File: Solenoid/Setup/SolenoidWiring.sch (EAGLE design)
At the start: 11 parts

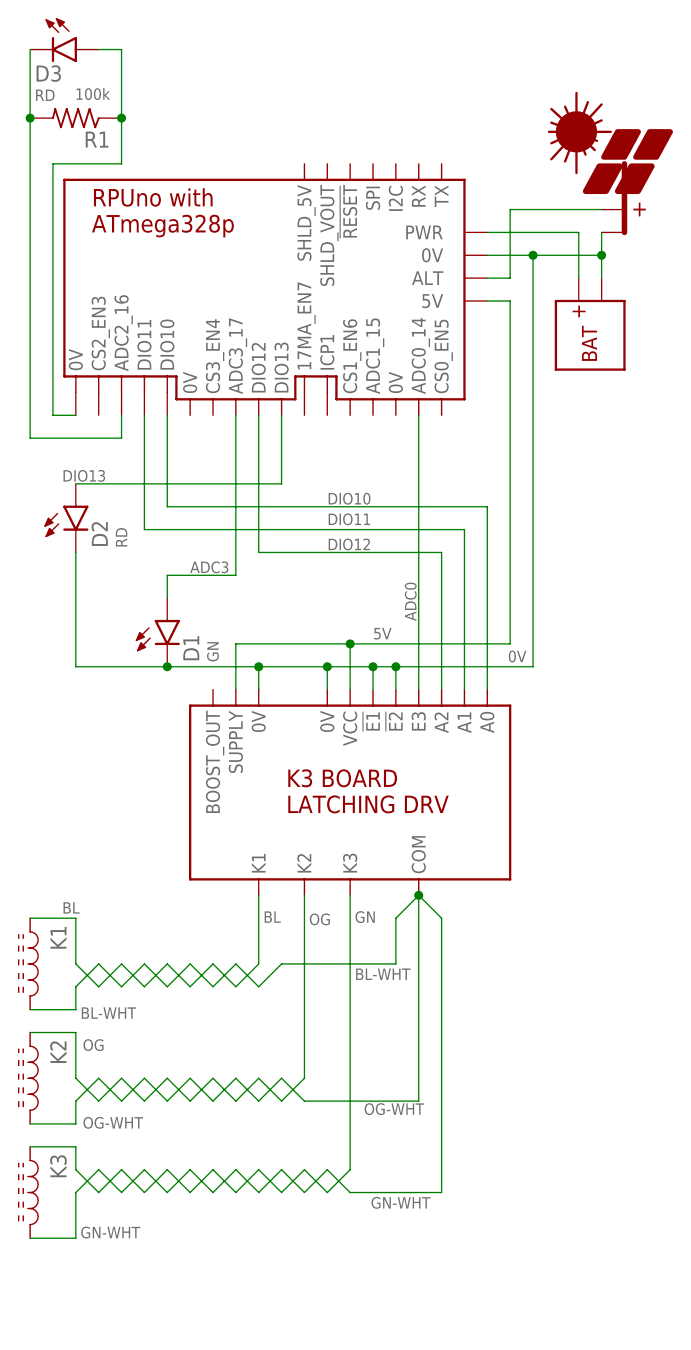
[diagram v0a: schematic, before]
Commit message: Solenoid: wiring show flow sensor
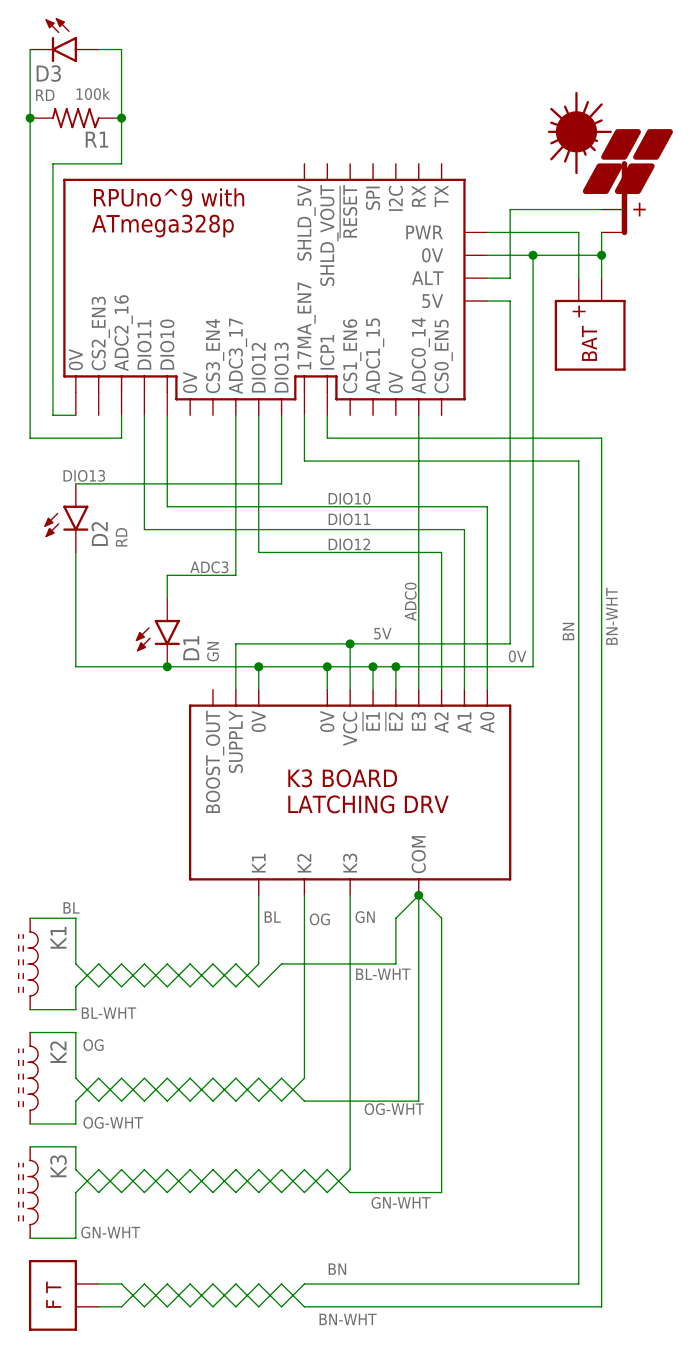
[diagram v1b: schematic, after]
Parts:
- added U$2: FT, Documentation:FT
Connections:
- new net BN: BM1.17MA_EN7, U$2.PWR
- new net BN-WHT: BM1.ICP1, U$2.PL
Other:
- note added: "FLOW SENSOR"
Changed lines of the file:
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@@
 <part name="D3" library="D-LED" deviceset="LED" device="5MM" value="RD"/>
 <part name="R1" library="R-C" deviceset="R" device="0805" value="100k"/>
+<part name="U$2" library="Documentation" deviceset="FT" device=""/>
 </parts>
 <sheets>
@@
 <text x="20.828" y="67.564" size="1.27" layer="98" rot="R90">DAY-NIGHT</text>
 <text x="8.89" y="116.84" size="1.27" layer="98" rot="R90">LIGHT SENSOR</text>
+<text x="17.78" y="-8.89" size="1.27" layer="98">FLOW SENSOR</text>
 </plain>
 <instances>
@@
 <instance part="D3" gate="G$1" x="15.24" y="134.62" rot="R270"/>
 <instance part="R1" gate="G$1" x="15.24" y="127" rot="R180"/>
+<instance part="U$2" gate="G$1" x="12.7" y="-2.54" rot="R270"/>
 </instances>
 <busses>
@@
 </segment>
 </net>
+<net name="BN-WHT" class="0">
+<segment>
+<pinref part="BM1" gate="G$1" pin="ICP1"/>
+<wire x1="43.18" y1="93.98" x2="43.18" y2="91.44" width="0.1524" layer="91"/>
+<pinref part="U$2" gate="G$1" pin="PL"/>
+<wire x1="43.18" y1="91.44" x2="73.66" y2="91.44" width="0.1524" layer="91"/>
+<wire x1="73.66" y1="91.44" x2="73.66" y2="-5.08" width="0.1524" layer="91"/>
+<wire x1="73.66" y1="-5.08" x2="40.64" y2="-5.08" width="0.1524" layer="91"/>
+<wire x1="40.64" y1="-5.08" x2="38.1" y2="-2.54" width="0.1524" layer="91"/>
+<wire x1="38.1" y1="-2.54" x2="35.56" y2="-5.08" width="0.1524" layer="91"/>
+<wire x1="35.56" y1="-5.08" x2="33.02" y2="-2.54" width="0.1524" layer="91"/>
+<wire x1="33.02" y1="-2.54" x2="30.48" y2="-5.08" width="0.1524" layer="91"/>
+<wire x1="30.48" y1="-5.08" x2="27.94" y2="-2.54" width="0.1524" layer="91"/>
+<wire x1="27.94" y1="-2.54" x2="25.4" y2="-5.08" width="0.1524" layer="91"/>
+<wire x1="25.4" y1="-5.08" x2="22.86" y2="-2.54" width="0.1524" layer="91"/>
+<wire x1="22.86" y1="-2.54" x2="20.32" y2="-5.08" width="0.1524" layer="91"/>
+<wire x1="20.32" y1="-5.08" x2="17.78" y2="-5.08" width="0.1524" layer="91"/>
+<label x="75.438" y="68.326" size="1.27" layer="91" rot="R90"/>
+<label x="42.164" y="-7.112" size="1.27" layer="91"/>
+</segment>
+</net>
+<net name="BN" class="0">
+<segment>
+<pinref part="U$2" gate="G$1" pin="PWR"/>
+<wire x1="17.78" y1="-2.54" x2="20.32" y2="-2.54" width="0.1524" layer="91"/>
+<wire x1="20.32" y1="-2.54" x2="22.86" y2="-5.08" width="0.1524" layer="91"/>
+<wire x1="22.86" y1="-5.08" x2="25.4" y2="-2.54" width="0.1524" layer="91"/>
+<wire x1="25.4" y1="-2.54" x2="27.94" y2="-5.08" width="0.1524" layer="91"/>
+<wire x1="27.94" y1="-5.08" x2="30.48" y2="-2.54" width="0.1524" layer="91"/>
+<wire x1="30.48" y1="-2.54" x2="33.02" y2="-5.08" width="0.1524" layer="91"/>
+<wire x1="33.02" y1="-5.08" x2="35.56" y2="-2.54" width="0.1524" layer="91"/>
+<wire x1="35.56" y1="-2.54" x2="38.1" y2="-5.08" width="0.1524" layer="91"/>
+<wire x1="38.1" y1="-5.08" x2="40.64" y2="-2.54" width="0.1524" layer="91"/>
+<wire x1="40.64" y1="-2.54" x2="71.12" y2="-2.54" width="0.1524" layer="91"/>
+<wire x1="71.12" y1="-2.54" x2="71.12" y2="88.9" width="0.1524" layer="91"/>
+<pinref part="BM1" gate="G$1" pin="17MA_EN7"/>
+<wire x1="71.12" y1="88.9" x2="40.64" y2="88.9" width="0.1524" layer="91"/>
+<wire x1="40.64" y1="88.9" x2="40.64" y2="93.98" width="0.1524" layer="91"/>
+<label x="70.612" y="68.834" size="1.27" layer="91" rot="R90"/>
+<label x="43.18" y="-1.524" size="1.27" layer="91"/>
+</segment>
+</net>
